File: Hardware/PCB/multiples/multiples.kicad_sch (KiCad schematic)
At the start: 37 parts, among them J1 AudioJack2_SwitchT, J10 AudioJack2, J11 AudioJack2, J2 Synth_power_2x5, J3 AudioJack2, J4 AudioJack2, J5 AudioJack2, J6 AudioJack2, J7 AudioJack2_SwitchT, J8 AudioJack2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

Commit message: KiCad 7, libraries to folder
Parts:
- removed TP2: +12V, ao_tht:TestPoint_THTPad_D1.5mm_Drill0.7mm, symbol ao_symbols:TestPoint
- removed TP3: GND, ao_tht:TestPoint_THTPad_1.5x1.5mm_Drill0.7mm, symbol ao_symbols:TestPoint
- added TP2: +12V, AO_tht:TestPoint_THTPad_D1.5mm_Drill0.7mm, symbol AO_symbols:TestPoint
- added TP3: GND, AO_tht:TestPoint_THTPad_D1.5mm_Drill0.7mm, symbol AO_symbols:TestPoint
- C1, C2: footprint ao_tht:CP_Radial_D6.3mm_P2.50mm -> AO_tht:CP_Radial_D6.3mm_P2.50mm; symbol Device:CP -> AO_symbols:CP
- C3, C4, C5, C6: footprint ao_tht:C_Disc_D3.0mm_W1.6mm_P2.50mm -> AO_tht:C_Disc_D3.0mm_W1.6mm_P2.50mm
- D1, D2: footprint ao_tht:D_DO-41_SOD81_P10.16mm_Horizontal -> AO_tht:D_DO-41_SOD81_P10.16mm_Horizontal
- GRAF1: symbol ao_symbols:Graphic -> AO_symbols:Graphic
- GRAF2: footprint ao_tht:analogoutput -> AO_tht:analogoutput; symbol ao_symbols:Graphic -> AO_symbols:Graphic
- GRAF3: footprint ao_tht:CC0_logo -> AO_tht:CC0_logo; symbol ao_symbols:Graphic -> AO_symbols:Graphic
- J1: footprint ao_tht:Jack_6.35mm_PJ_629HAN -> AO_tht:Jack_6.35mm_PJ_629HAN_slots; symbol Connector:AudioJack2_SwitchT -> AO_symbols:AudioJack2; SKU (none) -> A-1121; Vendor (none) -> Tayda
- J10, J11, J3, J4, J5, J6, J8, J9: footprint ao_tht:Jack_6.35mm_PJ_629HAN -> AO_tht:Jack_6.35mm_PJ_629HAN_slots; symbol Connector:AudioJack2 -> AO_symbols:AudioJack2; SKU (none) -> A-1121; Vendor (none) -> Tayda
- J2: footprint ao_tht:Power_Header -> AO_tht:Power_Header; symbol ao_symbols:Synth_power_2x5 -> AO_symbols:Synth_power_2x5
- J7: footprint ao_tht:Jack_6.35mm_PJ_629HAN -> AO_tht:Jack_6.35mm_PJ_629HAN_slots; symbol Connector:AudioJack2_SwitchT -> AO_symbols:AudioJack2_SwitchT; SKU (none) -> A-1121; Vendor (none) -> Tayda
- R1, R10, R2, R3, R4, R5, R6, R7, R8, R9: footprint ao_tht:R_Axial_DIN0207_L6.3mm_D2.5mm_P10.16mm_Horizontal -> AO_tht:R_Axial_DIN0207_L6.3mm_D2.5mm_P10.16mm_Horizontal
- TP1: footprint ao_tht:TestPoint_THTPad_D1.5mm_Drill0.7mm -> AO_tht:TestPoint_THTPad_D1.5mm_Drill0.7mm; symbol ao_symbols:TestPoint -> AO_symbols:TestPoint; Config (none) -> DNF
- U1, U2: footprint ao_tht:DIP-14_W7.62mm_Socket_LongPads -> AO_tht:DIP-14_W7.62mm_Socket_LongPads; symbol ao_symbols:TL074 -> AO_symbols:TL074
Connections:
- net +12V: now also TP2.1
- net GND: now also TP3.1; no longer J1.TN

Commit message: Pre fab tweaks
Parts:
- renumbered J2 to J1, J1 to J2

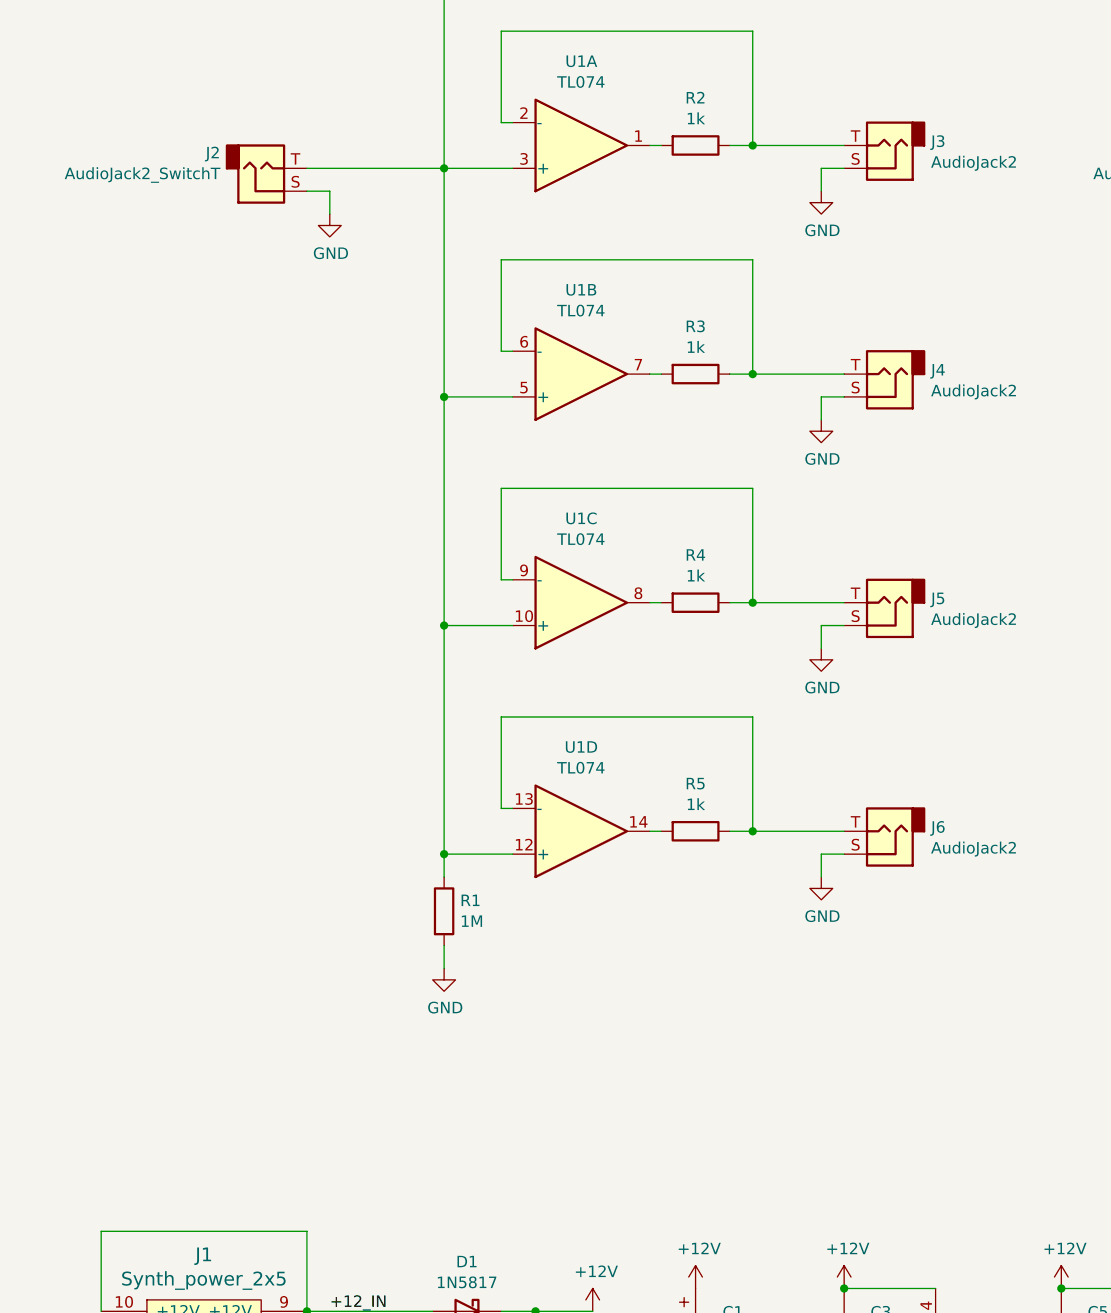
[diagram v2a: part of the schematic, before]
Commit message: DIP sockets; PDF docs; README
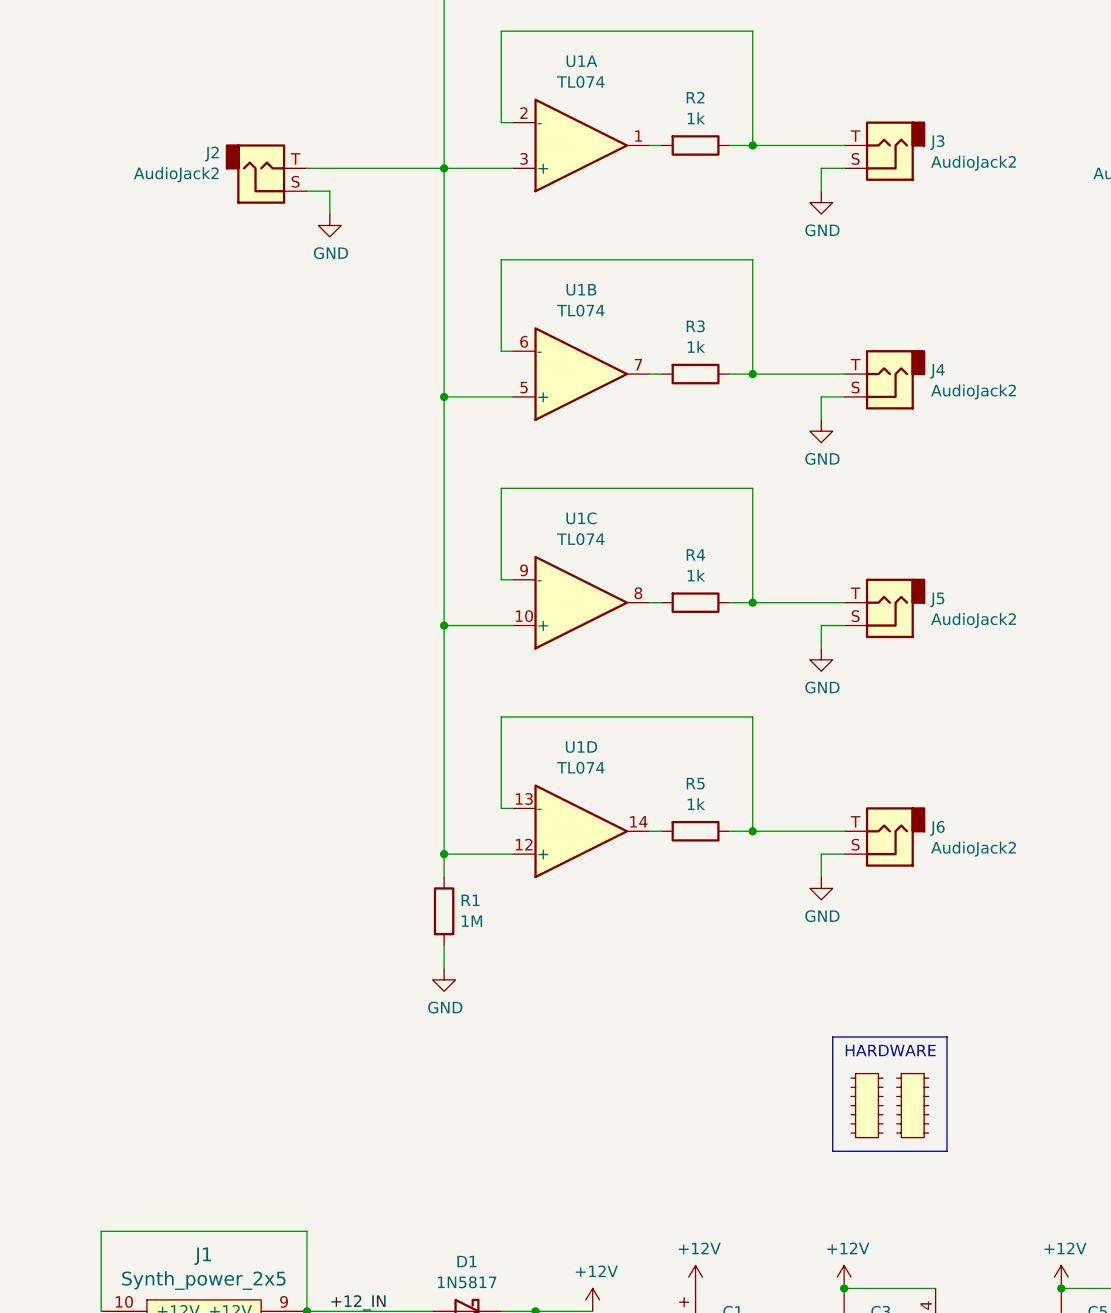
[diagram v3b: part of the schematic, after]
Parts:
- added J12, J13: DIP-14, symbol AO_symbols:DIP-14
- J2: value AudioJack2_SwitchT -> AudioJack2
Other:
- note added: "HARDWARE"
